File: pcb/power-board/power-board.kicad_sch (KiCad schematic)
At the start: 3 parts, among them J1 USB_C_Receptacle_USB2.0_16P

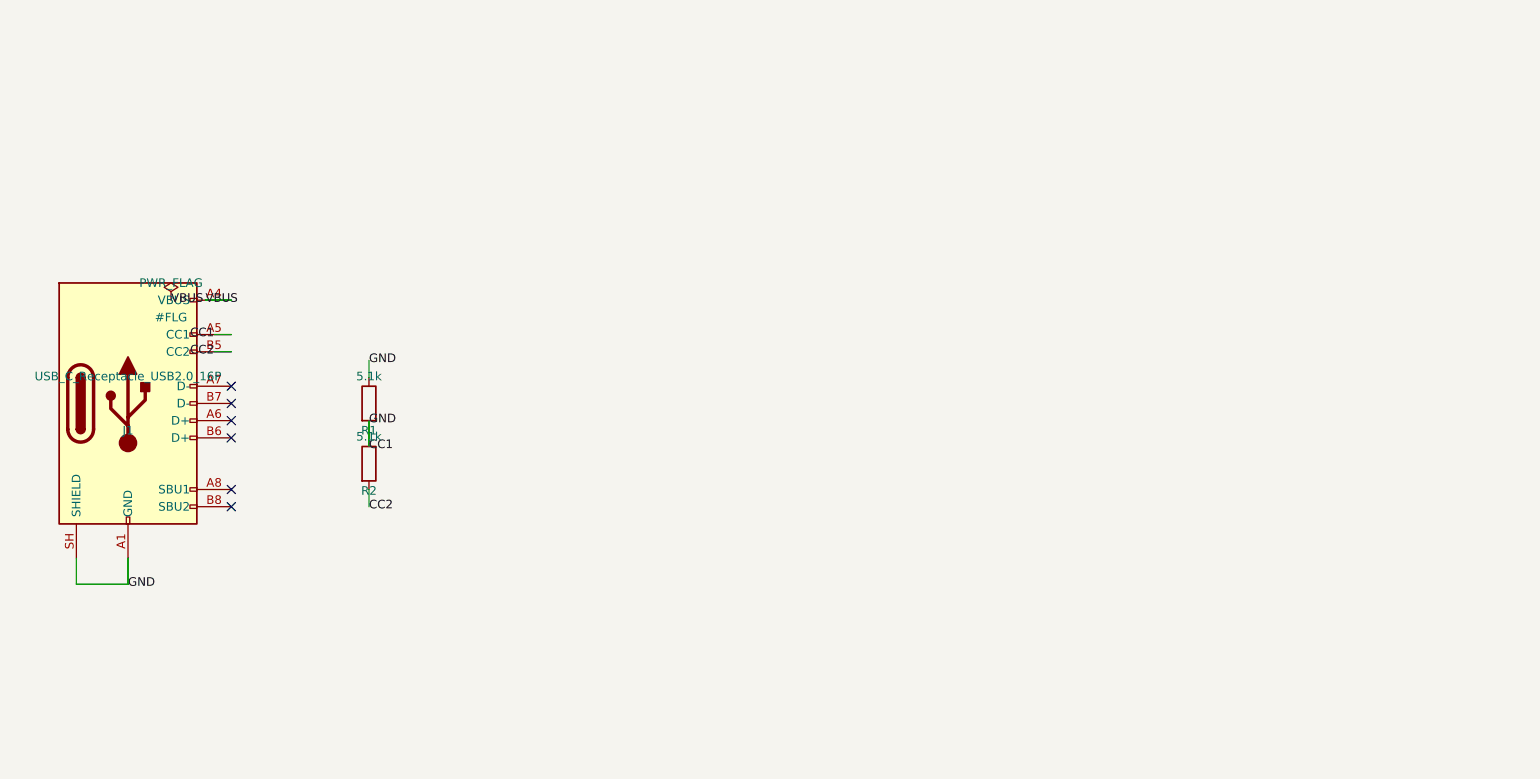
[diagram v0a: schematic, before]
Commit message: Phase 6: power board schematic complete, ERC error-free
Full power architecture captured in pcb/power-board/:
- J1 USB-C (16P) with 5.1k CC pulldowns, GND/SHIELD bus, PWR_FLAG on VBUS
- U1 BQ25895RTW charger: BAT/SYS/SW/REGN/PMID/BTST nets, ILIM via R3
  196R (KILIM 390 typ -> ~2A input limit), OTG pulldown R4, CE pullup
  R5 to REGN, I2C/STAT/INT pullups R6-R9 to REGN
- U2 DW01A + Q1 dual-NMOS pack protection in DW01A standard topology:
  PACKNEG(Q1.D1) -> FETMID(Q1.S1=D2) -> BATGND(Q1.S2), OD->G1, OC->G2
- U3 TPS62130 3.3V buck: SW33->L1 2.2uH->VOS33, FB tied to VOS33,
  FSW/DEF/SS tied to GND, VIN=BAT, exposed pad on GND
- J3 2x05 output header: VBUS, GND, BAT, EN33, STAT

ERC: 0 errors (kicad-cli sch erc --severity-error); 8 warnings are
single-pin nets intentionally left for the SBC-side connections
(USB D+/D-, I2C, TS NTC, DSEL/PMID/BTST passives).

Generator findings recorded in code:
- multi-unit symbols: DW01A pins live in _0_1 shared unit, dual FETs
  need one instance per unit (1=G1/S1/D1, 2=S2/G2/D2)
- same-potential pins share one sheet point (TPS62130 1/2/3, 10/11/12,
  6/15/16/17) - vertical jogs separate their stubs
- GND must be a power:GND symbol; a local label named GND does not
  merge with the global net and shorts BAT/GND in the netlist
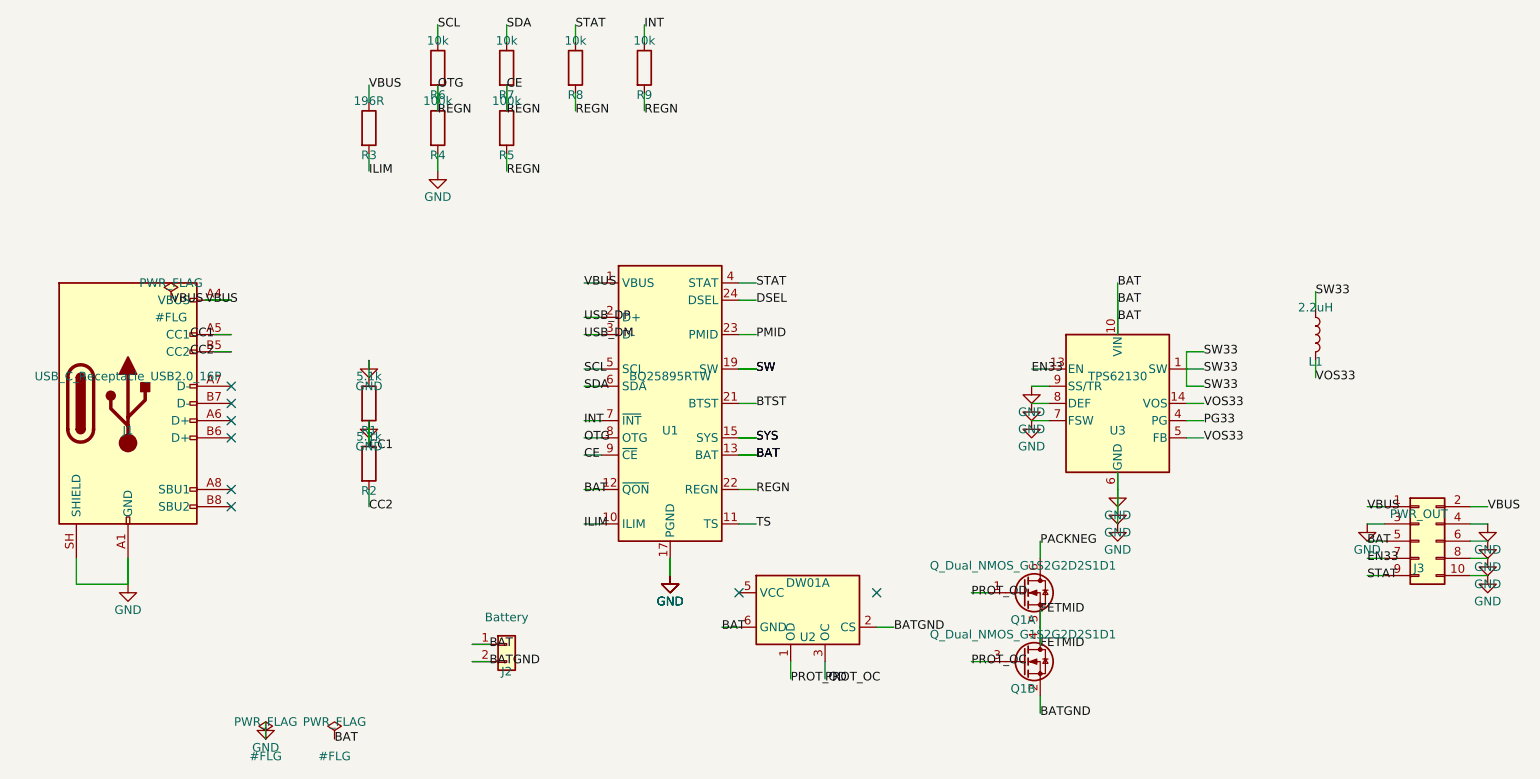
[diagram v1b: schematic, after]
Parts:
- added J2: Battery, Connector_JST:JST_PH_S2B-PH-K_1x02_P2.00mm_Horizontal, symbol Connector_Generic:Conn_01x02
- added J3: PWR_OUT, Connector_PinHeader_2.54mm:PinHeader_2x05_P2.54mm_Vertical, symbol Connector_Generic:Conn_02x05_Odd_Even
- added L1: 2.2uH, Inductor_SMD:L_0805_2012Metric, symbol Device:L
- added Q1: Q_Dual_NMOS_G1S2G2D2S1D1, Package_TO_SOT_SMD:SOT-23-6, symbol Transistor_FET:Q_Dual_NMOS_G1S2G2D2S1D1
- added R3: 196R, Resistor_SMD:R_0402_1005Metric, symbol Device:R
- added R4, R5: 100k, Resistor_SMD:R_0402_1005Metric, symbol Device:R
- added R6, R7, R8, R9: 10k, Resistor_SMD:R_0402_1005Metric, symbol Device:R
- added U1: BQ25895RTW, Package_DFN_QFN:Texas_RTW_WQFN-24-1EP_4x4mm_P0.5mm_EP2.7x2.7mm, symbol Battery_Management:BQ25895RTW
- added U2: DW01A, Package_TO_SOT_SMD:SOT-23-6, symbol Battery_Management:DW01A
- added U3: TPS62130, Package_DFN_QFN:VQFN-16-1EP_3x3mm_P0.5mm_EP1.45x1.45mm, symbol Regulator_Switching:TPS62130
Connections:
- net VBUS: now also J3.1 (Pin_1), J3.2 (Pin_2), R3.1, U1.1 (VBUS)
- net CC1 renamed GND
- net GND: now also J3.10 (Pin_10), J3.3 (Pin_3), J3.4 (Pin_4), J3.6 (Pin_6), J3.8 (Pin_8), R4.2, U1.17 (PGND), U1.18 (PGND), U1.25 (PGND), U3.15 (GND), U3.16 (GND), U3.17 (GND), U3.6 (GND), U3.7 (FSW), U3.8 (DEF), U3.9 (SS/TR)
- new net BAT: J2.1 (Pin_1), J3.5 (Pin_5), U1.12 (~{QON}), U1.13 (BAT), U1.14 (BAT), U2.6 (GND), U3.10 (VIN), U3.11 (VIN), U3.12 (VIN)
- new net BATGND: J2.2 (Pin_2), Q1.2 (S), U2.2 (CS)
- new net BTST: U1.21 (BTST)
- new net CE: R4.1, R5.1, R5.2, R6.2, R7.2, R8.2, R9.2, U1.22 (REGN), U1.8 (OTG), U1.9 (~{CE})
- new net DSEL: U1.24 (DSEL)
- new net EN33: J3.7 (Pin_7), U3.13 (EN)
- new net FETMID: Q1.4 (D), Q1.5 (S)
- new net ILIM: R3.2, U1.10 (ILIM)
- new net INT: R9.1, U1.7 (~{INT})
- new net PACKNEG: Q1.6 (D)
- new net PG33: U3.4 (PG)
- new net PMID: U1.23 (PMID)
- new net PROT_OC: Q1.3 (G), U2.3 (OC)
- new net PROT_OD: Q1.1 (G), U2.1 (OD)
- new net SCL: R6.1, U1.5 (SCL)
- new net SDA: R7.1, U1.6 (SDA)
- new net STAT: J3.9 (Pin_9), R8.1, U1.4 (STAT)
- new net SW: U1.19 (SW), U1.20 (SW)
- new net SW33: L1.1, U3.1 (SW), U3.2 (SW), U3.3 (SW)
- new net SYS: U1.15 (SYS), U1.16 (SYS)
- new net TS: U1.11 (TS)
- new net USB_DM: U1.3 (D-)
- new net USB_DP: U1.2 (D+)
- new net VOS33: L1.2, U3.14 (VOS), U3.5 (FB)
- no-connect marks 6 -> 8

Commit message: Phase 6: power board PCB placed, ERC 0 / DRC 0, STEP exported
pcb/power-board/power-board.kicad_pcb: 17 footprints placed (J1 USB-C,
U1 BQ25895, U2 DW01A, Q1 dual FET x2 units, U3 TPS62130, L1, J2/J3,
R1-R12, C1-C2), GND zone on B.Cu, KiCad-10 rule constraints in
board.design_settings.rules (min_hole_clearance 0.15 for the USB-C
shell NPTH geometry, min_via_diameter 0.4).

Schematic fixes this round:
- D+/D- and DSEL are explicit no-connects (charging-only, BC1.2 mux off)
- J2.2 is PACKNEG: battery negative routes through the protection FETs
  (previous wiring tied it to BATGND, bypassing Q1)
- C1 8.2uF PMID bypass, C2 47nF BTST-SW bootstrap, R10/R11 TS divider
  (bench bring-up; donor pack NTC replaces R11), R12 PG33 pullup
- PWR_FLAG references now unique (#FLG01..), silencing the annotation
  warning

Verification: kicad-cli sch erc --severity-all -> 0 violations;
pcb drc --severity-all -> 0 violations (56 ratsnest = routing pending);
STEP exported (U3 3D model missing - library has no VQFN-16 3x3 EP1.45
STEP; recorded as a sourcing item like U9).

Routing status: automatic routing still open. A naive L-router
shorted across the dense 0.5mm-pitch rows, so route_power_board.py
ships with --no-routes (placement + GND zone) and the switchbox
router as WIP. Board is an ESTIMATED 105x45mm exploratory envelope
pending donor measurements (U1-U5).
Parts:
- added C1: 8.2uF, Capacitor_SMD:C_0805_2012Metric, symbol Device:C
- added C2: 47nF, Capacitor_SMD:C_0402_1005Metric, symbol Device:C
- added R10, R11, R12: 10k, Resistor_SMD:R_0402_1005Metric, symbol Device:R
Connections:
- net BATGND: no longer J2.2 (Pin_2)
- net BTST: now also C2.1
- net CE: now also R10.1
- net GND: now also C1.2, R11.2
- net PACKNEG: now also J2.2 (Pin_2)
- net PG33: now also R12.1
- net PMID: now also C1.1
- net SW: now also C2.2
- net TS: now also R10.2, R11.1
- net VOS33: now also R12.2
- net DSEL: no longer names the net of U1.24 (DSEL)
- net USB_DM: no longer names the net of U1.3 (D-)
- net USB_DP: no longer names the net of U1.2 (D+)
- no-connect marks 8 -> 11

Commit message: Phase 6: U11 fix applied (STAT pull-up moved to Radxa side), DRC state recorded
- R8 (STAT 10k pull-up to REGN 4.7V) removed from the schematic:
  STAT is open-drain, its pull-up now lives on the Radxa side at
  3.3V per docs/harness-j3-radxa.md - prevents over-stressing the
  SBC GPIO (3.63V abs max).  ERC stays 0.
- PCB re-placed and re-routed through the pipeline.  DRC settles at
  7 via-track clearance violations (0.08-0.12mm measured) - the
  freerouting 1.6.2 via-padstack limitation documented in
  docs/drc-exceptions-power-board.md; interactive via relocation
  confirmed locally-optimal (each move trades one violation for
  another).
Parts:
- removed R8: 10k, Resistor_SMD:R_0402_1005Metric, symbol Device:R
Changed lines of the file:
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@@
-	(symbol
-		(lib_id "Device:R")
-		(at 185.42 30.48 0)
-		(unit 1)
-		(exclude_from_sim no)
-		(in_bom yes)
-		(on_board yes)
-		(dnp no)
-		(property "Reference" "R8"
-			(at 185.42 34.48 0)
-			(effects (font (size 1.27 1.27)))
-		)
-		(property "Value" "10k"
-			(at 185.42 26.48 0)
-			(effects (font (size 1.27 1.27)))
-		)
-		(property "Footprint" "Resistor_SMD:R_0402_1005Metric"
-			(at 185.42 30.48 0)
-			(effects (font (size 1.27 1.27)) (hide yes))
-		)
-		(property "Datasheet" "~"
-			(at 185.42 30.48 0)
-			(effects (font (size 1.27 1.27)) (hide yes))
-		)
-		(property "Description" "10k"
-			(at 185.42 30.48 0)
-			(effects (font (size 1.27 1.27)) (hide yes))
-		)
-		(pin "1"
-		)
-		(pin "2"
-		)
-		(instances
-			(project "power-board"
-				(path "/d1e2f3a4-5b6c-4d7e-8f90-a1b2c3d4e5f6"
-					(reference "R8")
-					(unit 1)
-				)
-			)
-		)
-	)
-	(wire
-		(pts (xy 185.42 26.67) (xy 185.42 24.13))
-		(stroke (width 0) (type default))
-	)
-	(label "STAT"
-		(at 185.42 24.13 0)
-		(effects (font (size 1.27 1.27)))
-	)
-	(wire
-		(pts (xy 185.42 34.29) (xy 185.42 36.83))
-		(stroke (width 0) (type default))
-	)
-	(label "REGN"
-		(at 185.42 36.83 0)
-		(effects (font (size 1.27 1.27)))
-	)
 	(symbol
 		(lib_id "Device:R")
